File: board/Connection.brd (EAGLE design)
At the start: 159.7 x 100.3 mm, 42 parts, among them U1 NUCLEO-G431KB, U2 SN65HVD230, U5 ADA4528-1ARMZ-R7

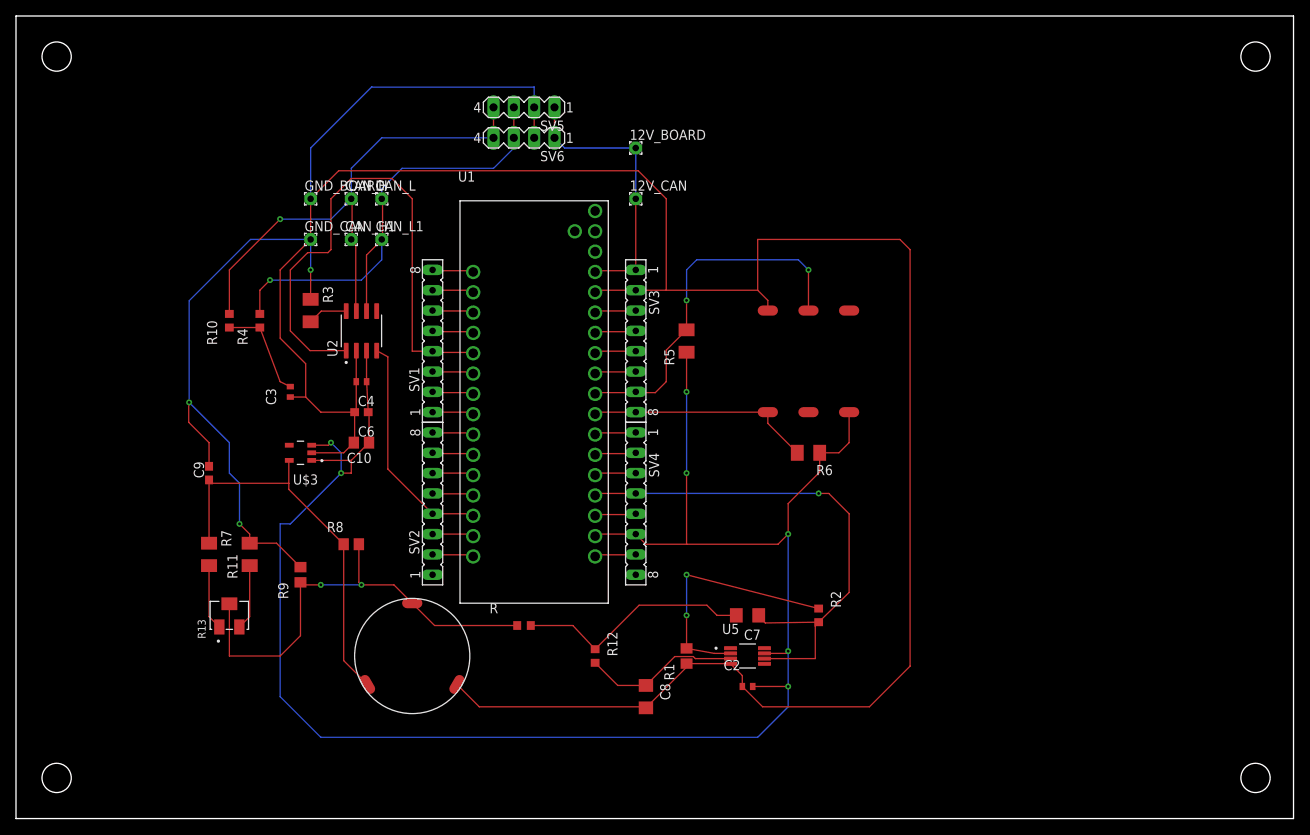
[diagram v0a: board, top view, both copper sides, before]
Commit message: move ch4 sensor away from nucleo female header pins for nucleo insertion move the 4pin CAN away from top of the nucleo space the other CAN pins to fit a terminal block
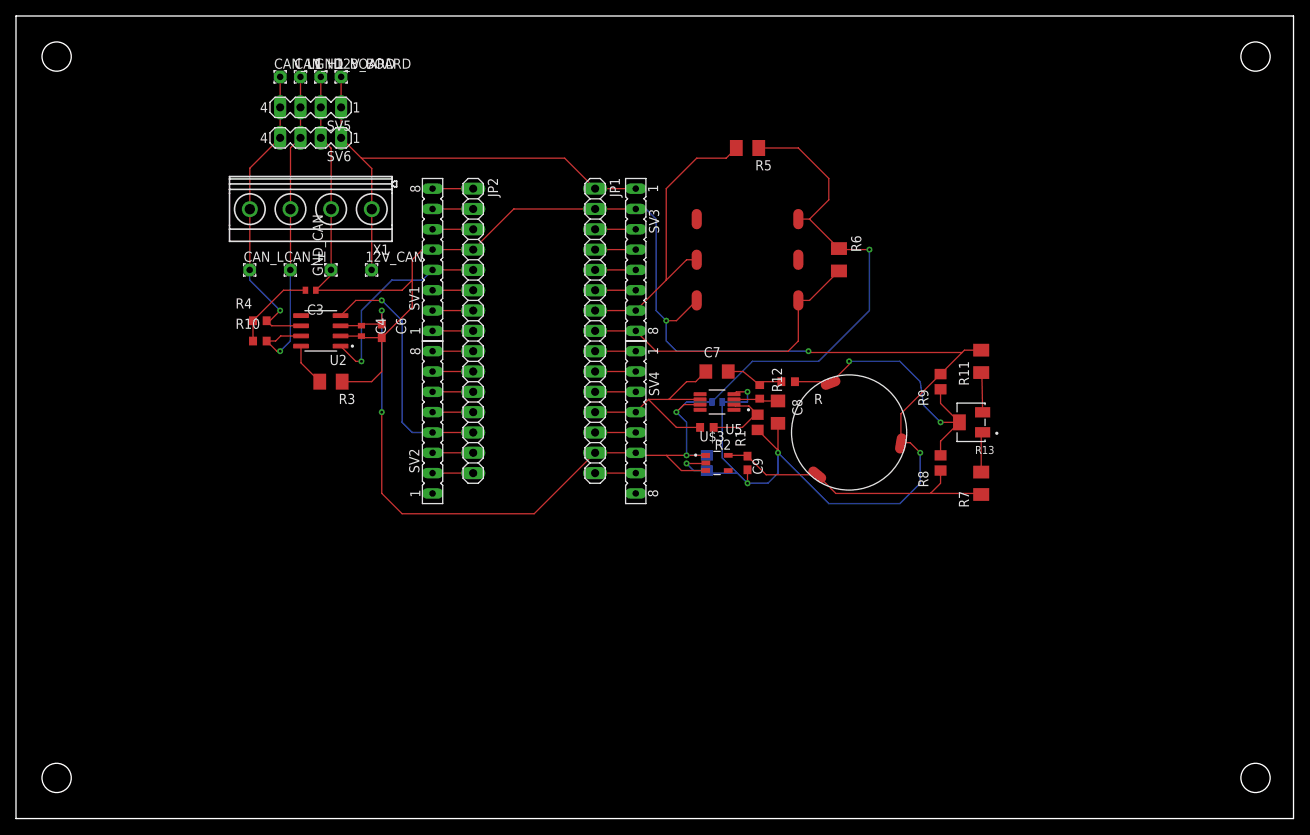
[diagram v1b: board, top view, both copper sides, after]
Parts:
- removed U1: NUCLEO-G431KB, NUCLEO-G431KB:MODULE_NUCLEO-G431KB
- added JP1, JP2: (no value), pinhead:1X15
- added X1: MKDSN1,5/4-5,08, con-phoenix-508:MKDSN1,5/4-5,08
- moved R7 96.9 mm to (106.7, 29.2), turned to 90 degrees
- moved R13 95.8 mm to (105.4, 36.8), turned to 180 degrees
- moved R11 94.6 mm to (106.7, 44.5)
- moved R9 83.6 mm to (101.6, 41.9)
- moved R8 74.4 mm to (101.6, 31.8), turned to 90 degrees
- moved C9 67.3 mm to (77.5, 31.8), turned to 270 degrees
- moved U$1 61.3 mm to (90.2, 35.6), turned to 20.5 degrees
- moved U$3 52.1 mm to (73.7, 31.8), turned to 0 degrees
- moved R 44.9 mm to (82.5, 41.9), turned to 180 degrees
- moved C10 43.3 mm to (72.4, 31.8), flipped to the bottom, turned to 270 degrees
- moved C8 39.2 mm to (81.3, 38.1)
- moved R12 38.9 mm to (79.0, 40.6)
- moved 12V_BOARD 37.9 mm to (26.7, 80.0)
- moved C2 35.8 mm to (73.7, 39.4), flipped to the bottom
- moved 12V_CAN 34.2 mm to (30.5, 55.9)
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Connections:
- removed net N$30: SV1.5, U1.CN4_4
- net +12V: now also JP1.1, X1.1; no longer U1.CN3_1
- net 3V3: now also JP1.14; no longer U1.CN3_14
- net ADC: now also JP1.12; no longer U1.CN3_12
- net CANH: now also SV5.3, SV6.3, X1.3; no longer SV5.4, SV6.4
- net CANL: now also SV5.4, SV6.4, X1.4; no longer SV5.3, SV6.3
- net GND: now also JP1.2, JP2.4, SV1.5, X1.2; no longer U1.CN3_2
- net N$18: now also JP1.3; no longer U1.CN3_3
- net N$19: now also JP1.4; no longer U1.CN3_4
- net N$20: now also JP1.5; no longer U1.CN3_5
- net N$22: now also JP1.9; no longer U1.CN3_9
- net N$23: now also JP1.10; no longer U1.CN3_10
- net N$24: now also JP1.11; no longer U1.CN3_11
- net N$25: now also JP1.13; no longer U1.CN3_13
- net N$26: now also JP1.15; no longer U1.CN3_15
- net N$27: now also JP2.8; no longer U1.CN4_8
- net N$28: now also JP2.7; no longer U1.CN4_7
- net N$29: now also JP2.6; no longer U1.CN4_6
- net N$31: now also JP2.3; no longer U1.CN4_3
- net N$32: now also JP2.2; no longer U1.CN4_2
- net N$33: now also JP2.1; no longer U1.CN4_1
- net N$34: now also JP2.15; no longer U1.CN4_15
- net N$35: now also JP2.14; no longer U1.CN4_14
- net N$36: now also JP2.12; no longer U1.CN4_12
- net N$37: now also JP2.11; no longer U1.CN4_11
- net N$38: now also JP2.10; no longer U1.CN4_10
- net N$39: now also JP2.9; no longer U1.CN4_9
- net N$6: now also JP1.6; no longer U1.CN3_6
- net RX: now also JP2.13; no longer U1.CN4_13
- net SCL: now also JP1.7; no longer U1.CN3_7
- net SDA: now also JP1.8; no longer U1.CN3_8
- net TX: now also JP2.5; no longer U1.CN4_5
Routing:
- net GND: track 399.6 -> 247.2 mm, vias 3 -> 7
- net 3V3: track 226.7 -> 156.1 mm, vias 7 -> 5
- net TX: track 67.2 -> 25.8 mm, vias 0 -> 1
- net ADC: track 67.3 -> 27.8 mm, vias 1 -> 0
- net +12V: track 35.0 -> 61.6 mm
- net CANH: track 65.9 -> 42.1 mm
- net CANL: track 62.3 -> 39.1 mm
- net IN-: track 31.8 -> 9.55 mm, vias 2 -> 0
- net F1: track 29.8 -> 7.62 mm
- net OUTPUT: track 57.7 -> 36.7 mm
- net IN+: track 19.7 -> 5.90 mm
- net 3V: track 50.0 -> 37.0 mm
- net SDA: track 28.3 -> 38.7 mm
- net SCL: track 46.1 -> 37.6 mm, vias 2 -> 0
- net N$30: track 5.24 -> 0.00 mm
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
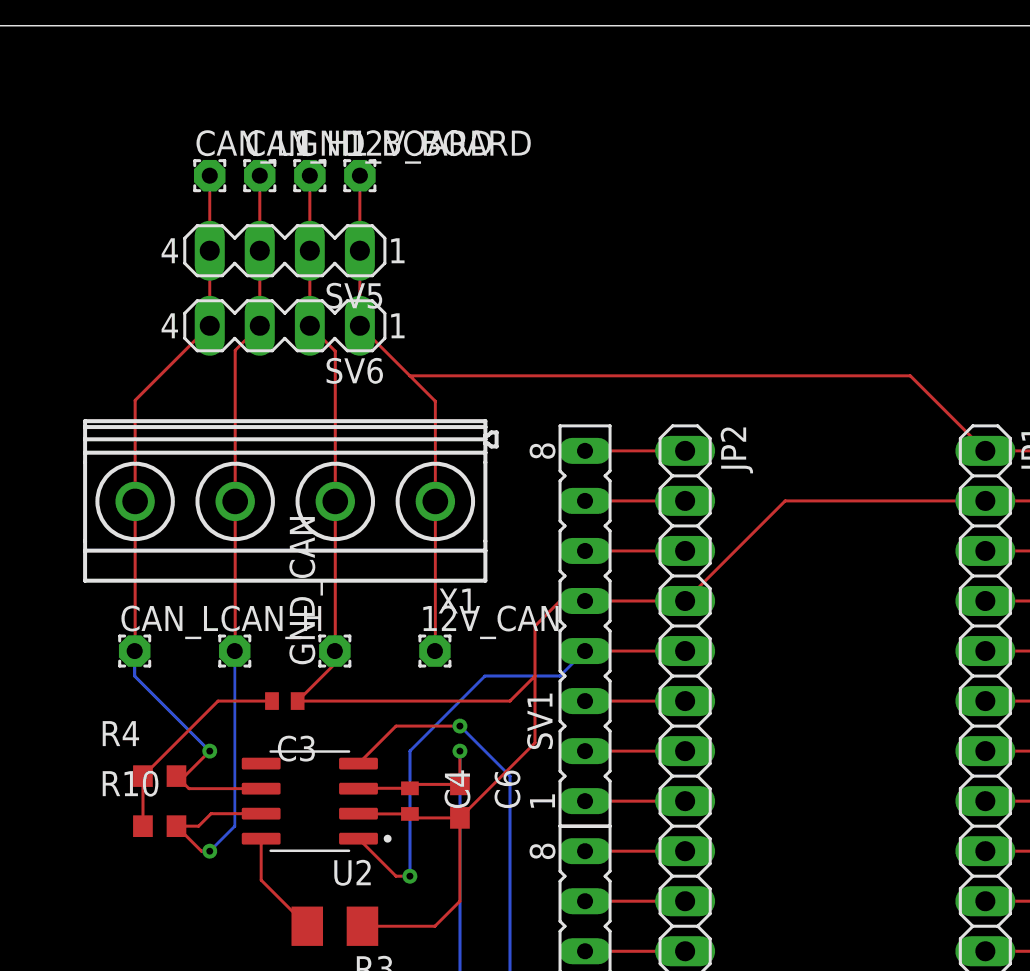
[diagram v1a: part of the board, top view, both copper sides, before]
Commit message: Used power terminal
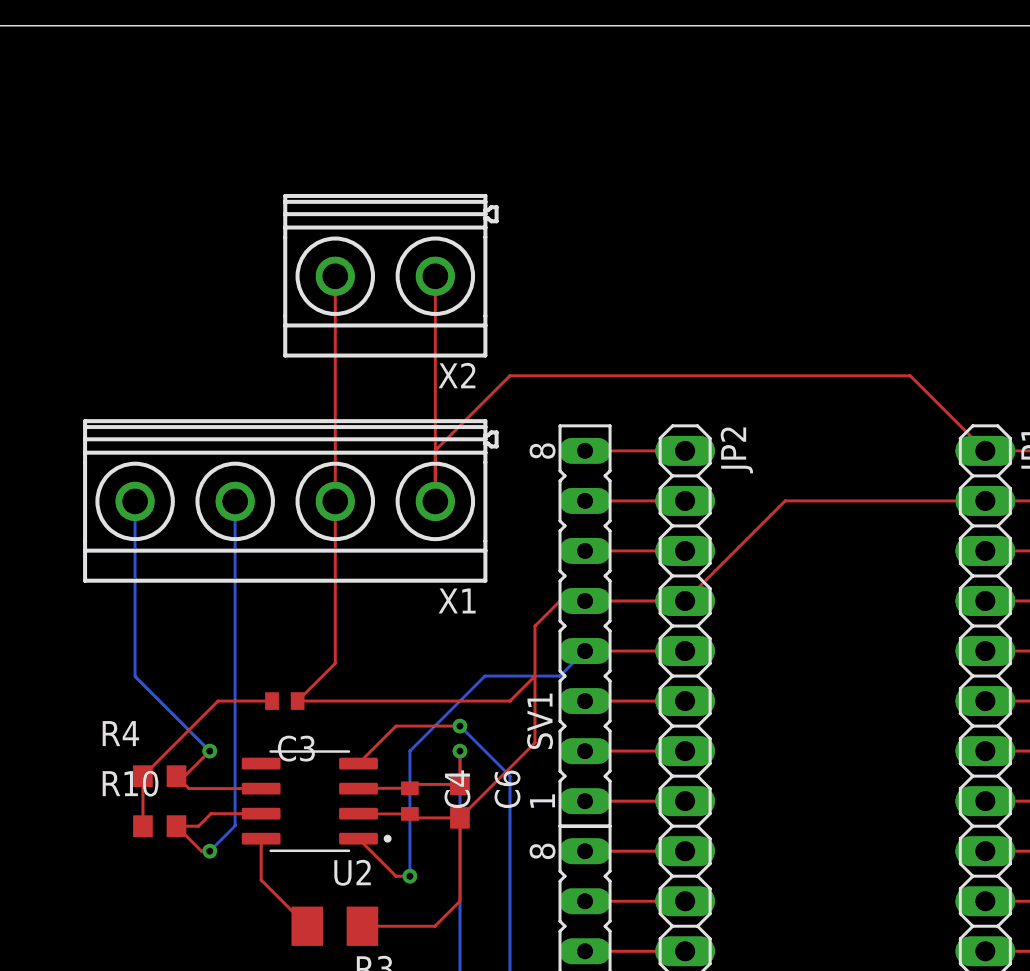
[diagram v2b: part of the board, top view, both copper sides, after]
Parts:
- removed 12V_BOARD, 12V_CAN: 12V, wirepad:1,6/0,8
- removed CAN_H, CAN_H1, CAN_L, CAN_L1, GND_BOARD, GND_CAN: (no value), wirepad:1,6/0,8
- removed SV5, SV6: (no value), con-lstb:MA04-1
- added X2: MKDSN1,5/2-5,08, con-phoenix-508:MKDSN1,5/2-5,08
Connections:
- net +12V: now also X2.1; no longer 12V_BOARD.1, 12V_CAN.1, SV5.1, SV6.1
- net CANH: no longer CAN_H.1, CAN_H1.1, SV5.3, SV6.3
- net CANL: no longer CAN_L.1, CAN_L1.1, SV5.4, SV6.4
- net GND: now also X2.2; no longer GND_BOARD.1, GND_CAN.1, SV5.2, SV6.2
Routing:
- net CANL: track 39.1 -> 21.0 mm
- net CANH: track 42.1 -> 25.1 mm
- net +12V: track 61.6 -> 50.2 mm
- net GND: track 247.2 -> 241.6 mm

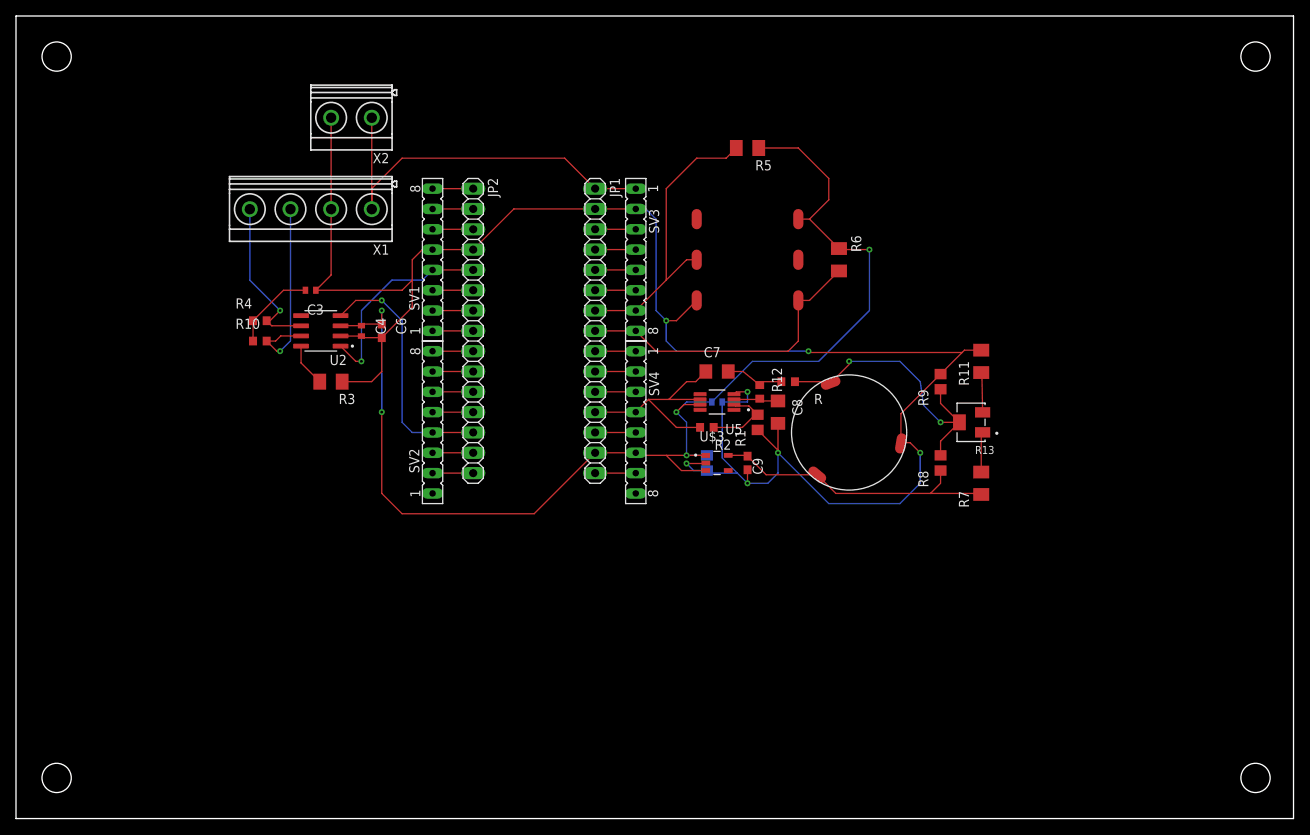
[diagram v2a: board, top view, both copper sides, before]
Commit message: Optimized the size of PCB
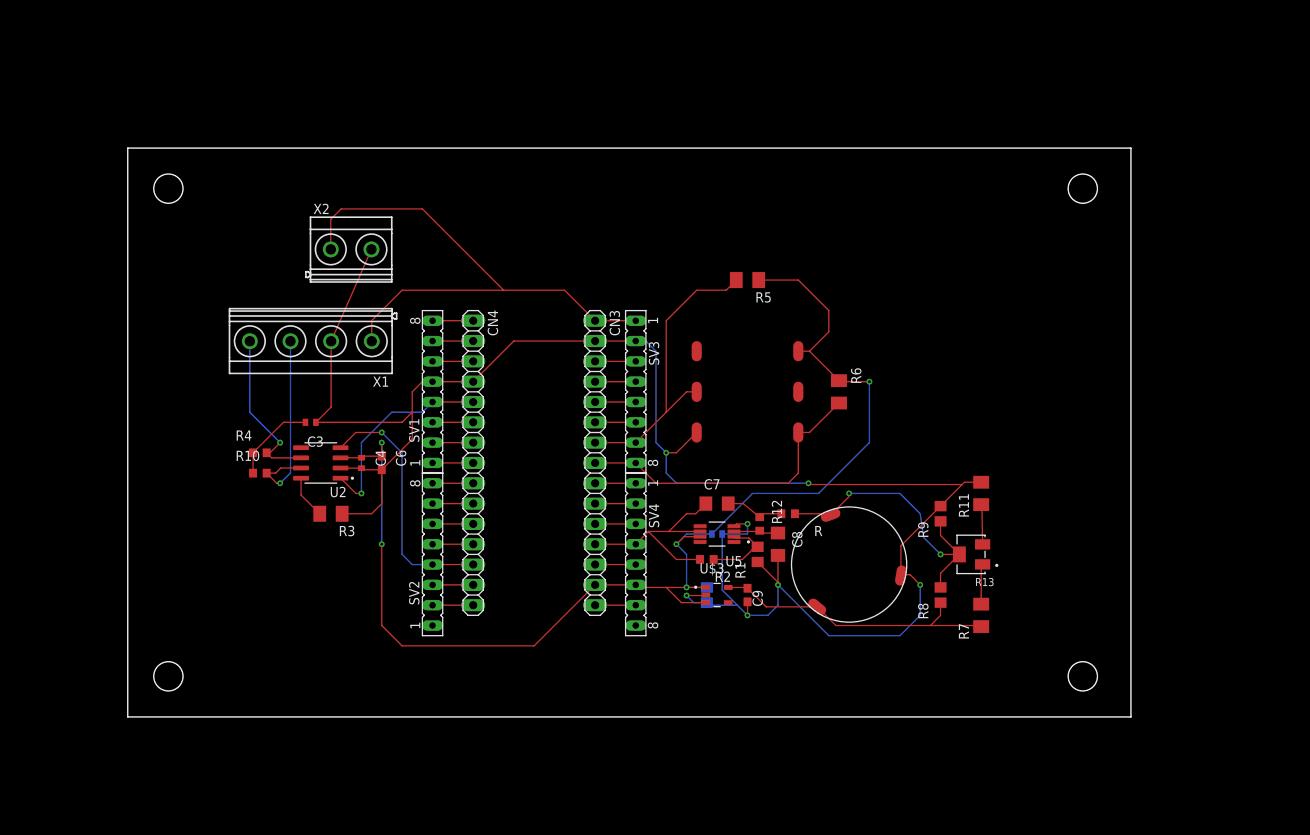
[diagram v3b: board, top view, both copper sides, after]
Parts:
- removed JP1, JP2: (no value), pinhead:1X15
- added CN3: CN3, pinhead:1X15
- added CN4: CN4, pinhead:1X15
- moved C3 16.5 mm to (22.9, 36.8)
- moved R5 16.5 mm to (77.5, 54.6)
- moved X2 16.5 mm to (27.9, 58.4), turned to 0 degrees
- moved C8 16.5 mm to (81.3, 21.6)
- moved R10 16.5 mm to (16.5, 30.5)
- moved R11 16.5 mm to (106.7, 27.9)
- moved R12 16.5 mm to (79.0, 24.1)
- moved R2 16.5 mm to (72.4, 19.7)
- moved R7 16.5 mm to (106.7, 12.7)
- moved U$1 16.5 mm to (90.2, 19.1)
- moved C10 16.5 mm to (72.4, 15.2)
- moved C2 16.5 mm to (73.7, 22.9)
- moved C4 16.5 mm to (29.2, 31.8)
- moved C6 16.5 mm to (31.8, 31.8)
- moved C7 16.5 mm to (73.7, 26.7)
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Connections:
- net +12V: now also CN3.1; no longer JP1.1
- net 3V3: now also CN3.14; no longer JP1.14
- net ADC: now also CN3.12; no longer JP1.12
- net GND: now also CN3.2, CN4.4; no longer JP1.2, JP2.4
- net N$18: now also CN3.3; no longer JP1.3
- net N$19: now also CN3.4; no longer JP1.4
- net N$20: now also CN3.5; no longer JP1.5
- net N$22: now also CN3.9; no longer JP1.9
- net N$23: now also CN3.10; no longer JP1.10
- net N$24: now also CN3.11; no longer JP1.11
- net N$25: now also CN3.13; no longer JP1.13
- net N$26: now also CN3.15; no longer JP1.15
- net N$27: now also CN4.8; no longer JP2.8
- net N$28: now also CN4.7; no longer JP2.7
- net N$29: now also CN4.6; no longer JP2.6
- net N$31: now also CN4.3; no longer JP2.3
- net N$32: now also CN4.2; no longer JP2.2
- net N$33: now also CN4.1; no longer JP2.1
- net N$34: now also CN4.15; no longer JP2.15
- net N$35: now also CN4.14; no longer JP2.14
- net N$36: now also CN4.12; no longer JP2.12
- net N$37: now also CN4.11; no longer JP2.11
- net N$38: now also CN4.10; no longer JP2.10
- net N$39: now also CN4.9; no longer JP2.9
- net N$6: now also CN3.6; no longer JP1.6
- net RX: now also CN4.13; no longer JP2.13
- net SCL: now also CN3.7; no longer JP1.7
- net SDA: now also CN3.8; no longer JP1.8
- net TX: now also CN4.5; no longer JP2.5
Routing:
- net +12V: track 50.2 -> 68.9 mm
- net GND: track 241.6 -> 242.7 mm
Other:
- board size 159.7 x 100.3 mm -> 125.4 x 71.1 mm
